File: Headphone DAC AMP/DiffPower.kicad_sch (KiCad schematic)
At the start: 0 parts

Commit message: Updating Changes
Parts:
- added U6: MCP1727-1802xSN, Package_SO:SOIC-8_3.9x4.9mm_P1.27mm, symbol Regulator_Linear:MCP1727-1802xSN
- added U7: MCP1727-3302xSN, Package_SO:SOIC-8_3.9x4.9mm_P1.27mm, symbol Regulator_Linear:MCP1727-3302xSN
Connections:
- new net: U7.1 (Vin), U7.2 (Vin)
- new net: U6.1 (Vin), U6.2 (Vin)
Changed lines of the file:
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@@
 	(generator_version "9.0")
 	(paper "A4")
+	(symbol
+		(lib_id "Regulator_Linear:MCP1727-3302xSN")
+		(at 71.12 99.06 0)
+		(unit 1)
+		(exclude_from_sim no)
+		(in_bom yes)
+		(on_board yes)
+		(dnp no)
+		(fields_autoplaced yes)
+		(property "Reference" "U7"
+			(at 71.12 88.9 0)
+			(effects
+				(font
+					(size 1.27 1.27)
+				)
+			)
+		)
+		(property "Value" "MCP1727-3302xSN"
+			(at 71.12 91.44 0)
+			(effects
+				(font
+					(size 1.27 1.27)
+				)
+			)
+		)
+		(property "Footprint" "Package_SO:SOIC-8_3.9x4.9mm_P1.27mm"
+			(at 71.12 74.93 0)
+			(effects
+				(font
+					(size 1.27 1.27)
+				)
+				(hide yes)
+			)
+		)
+		(property "Datasheet" "https://ww1.microchip.com/downloads/aemtest/APID/ProductDocuments/DataSheets/MCP1727-1.5A-Low-Voltage-Low-Quiescent-Current-LDO-Regulator-20001999D.pdf"
+			(at 71.12 77.47 0)
+			(effects
+				(font
+					(size 1.27 1.27)
+				)
+				(hide yes)
+			)
+		)
+		(property "Description" "1.5A, Low Voltage, Low Quiescent Current LDO Regulator, 2.3 - 6V Input, Fixed 3.3V Output, 330mV Dropout, SOIC-8"
+			(at 71.12 99.06 0)
+			(effects
+				(font
+					(size 1.27 1.27)
+				)
+				(hide yes)
+			)
+		)
+		(pin "8"
+		)
+		(pin "5"
+		)
+		(pin "2"
+		)
+		(pin "3"
+		)
+		(pin "4"
+		)
+		(pin "1"
+		)
+		(pin "7"
+		)
+		(pin "6"
+		)
+		(instances
+			(project ""
+				(path "/d034eddd-efbc-47be-a25c-37cbfbab4cd8/a76b11f7-fbf9-4331-be15-052b46a69f96"
+					(reference "U7")
+					(unit 1)
+				)
+			)
+		)
+	)
+	(symbol
+		(lib_id "Regulator_Linear:MCP1727-1802xSN")
+		(at 69.85 50.8 0)
+		(unit 1)
+		(exclude_from_sim no)
+		(in_bom yes)
+		(on_board yes)
+		(dnp no)
+		(fields_autoplaced yes)
+		(property "Reference" "U6"
+			(at 69.85 40.64 0)
+			(effects
+				(font
+					(size 1.27 1.27)
+				)
+			)
+		)
+		(property "Value" "MCP1727-1802xSN"
+			(at 69.85 43.18 0)
+			(effects
+				(font
+					(size 1.27 1.27)
+				)
+			)
+		)
+		(property "Footprint" "Package_SO:SOIC-8_3.9x4.9mm_P1.27mm"
+			(at 69.85 26.67 0)
+			(effects
+				(font
+					(size 1.27 1.27)
+				)
+				(hide yes)
+			)
+		)
+		(property "Datasheet" "https://ww1.microchip.com/downloads/aemtest/APID/ProductDocuments/DataSheets/MCP1727-1.5A-Low-Voltage-Low-Quiescent-Current-LDO-Regulator-20001999D.pdf"
+			(at 69.85 29.21 0)
+			(effects
+				(font
+					(size 1.27 1.27)
+				)
+				(hide yes)
+			)
+		)
+		(property "Description" "1.5A, Low Voltage, Low Quiescent Current LDO Regulator, 2.3 - 6V Input, Fixed 1.8V Output, 330mV Dropout, SOIC-8"
+			(at 69.85 50.8 0)
+			(effects
+				(font
+					(size 1.27 1.27)
+				)
+				(hide yes)
+			)
+		)
+		(pin "2"
+		)
+		(pin "8"
+		)
+		(pin "4"
+		)
+		(pin "5"
+		)
+		(pin "1"
+		)
+		(pin "3"
+		)
+		(pin "6"
+		)
+		(pin "7"
+		)
+		(instances
+			(project ""
+				(path "/d034eddd-efbc-47be-a25c-37cbfbab4cd8/a76b11f7-fbf9-4331-be15-052b46a69f96"
+					(reference "U6")
+					(unit 1)
+				)
+			)
+		)
+	)
 )

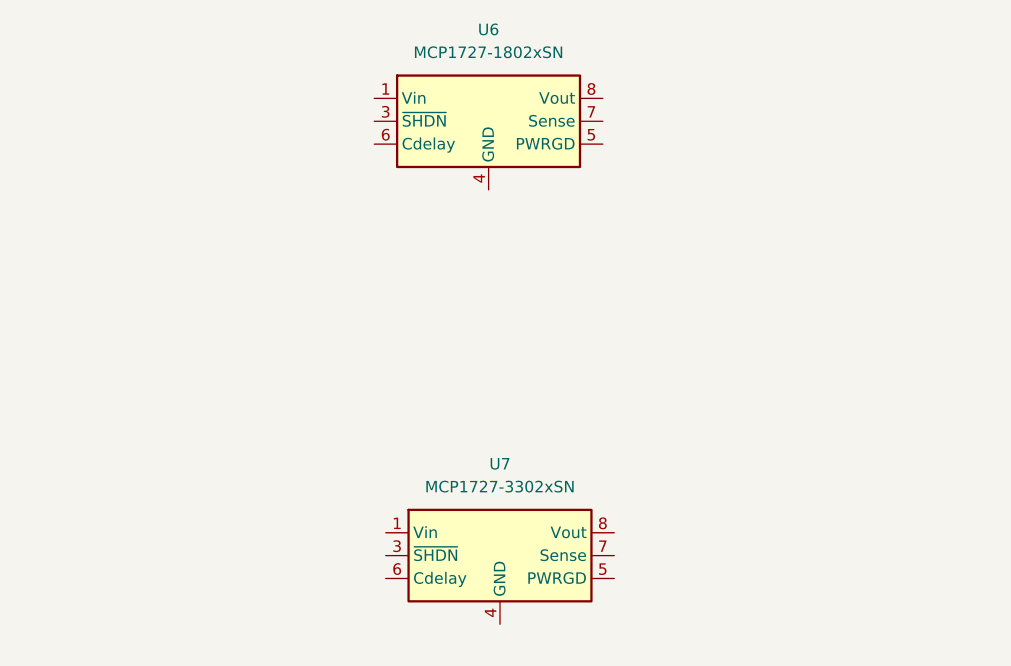
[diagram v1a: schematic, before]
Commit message: LDO Low Noise Rails 3.3 and 1.8
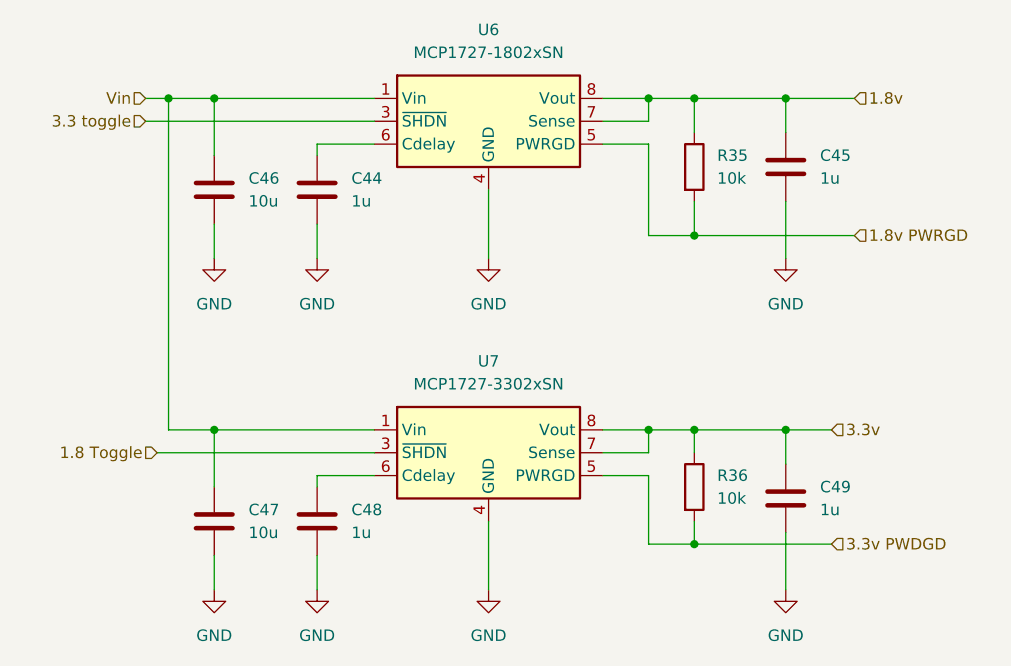
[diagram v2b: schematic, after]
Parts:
- added C44, C45, C48, C49: 1u, symbol Device:C
- added C46, C47: 10u, symbol Device:C
- added R35, R36: 10k, symbol Device:R
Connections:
- net Vin: now reaches U7.1 (Vin), U7.2 (Vin)
- net Vin: now also U6.1 (Vin), U6.2 (Vin), C46.1, C47.1
- net 1.8 Toggle: now reaches U7.3 (~{SHDN})
- net GND: now reaches U7.4 (GND)
- net GND: now also U6.4 (GND), C44.2, C45.2, C46.2, C47.2, C48.2, C49.2
- net 3.3v PWDGD: now reaches U7.5 (PWRGD)
- net 3.3v PWDGD: now also R36.2
- net at U7.6 (Cdelay): now also C48.1
- net 3.3v: now reaches U7.7 (Sense)
- net 3.3v: now also U7.8 (Vout), C49.1, R36.1
- net 3.3 toggle: now reaches U6.3 (~{SHDN})
- net 1.8v PWRGD: now reaches U6.5 (PWRGD)
- net 1.8v PWRGD: now also R35.2
- net at U6.6 (Cdelay): now also C44.1
- net 1.8v: now reaches U6.7 (Sense)
- net 1.8v: now also U6.8 (Vout), C45.1, R35.1
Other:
- moved on the sheet: U7

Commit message: Completed a significant amount of the power and routing
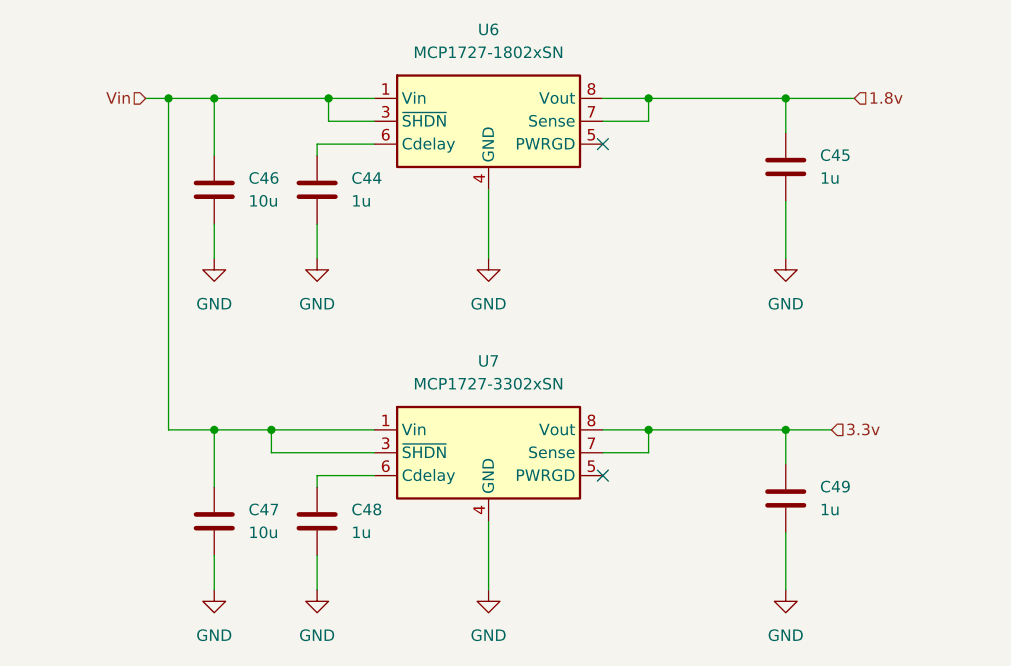
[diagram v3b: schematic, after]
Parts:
- removed R35, R36: 10k, symbol Device:R
- C44, C45, C46, C47, C48, C49: footprint (none) -> Capacitor_SMD:C_0805_2012Metric_Pad1.18x1.45mm_HandSolder
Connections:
- net 1.8 Toggle is gone; now on net Vin: U7.3 (~{SHDN})
- net 3.3 toggle is gone; now on net Vin: U6.3 (~{SHDN})
- net 1.8v PWRGD: no longer names the net of U6.5 (PWRGD)
- net 3.3v PWDGD: no longer names the net of U7.5 (PWRGD)
- no-connect marks 0 -> 2

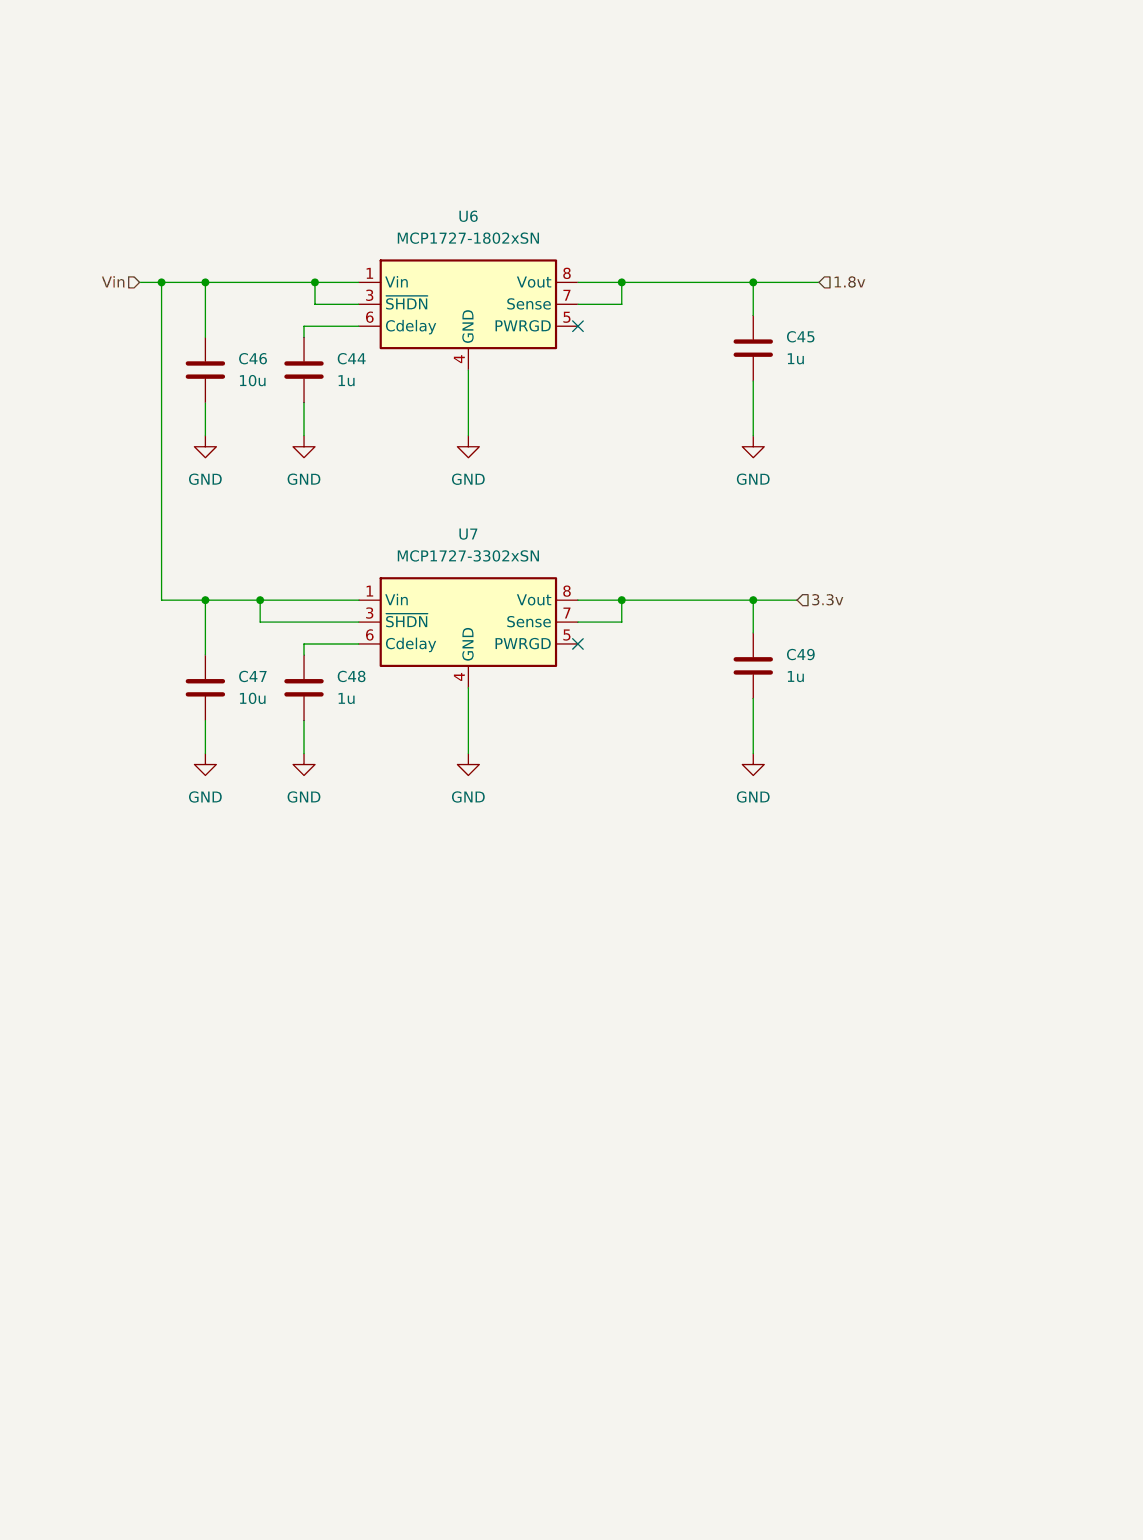
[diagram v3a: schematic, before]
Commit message: Added ground and 0.9v
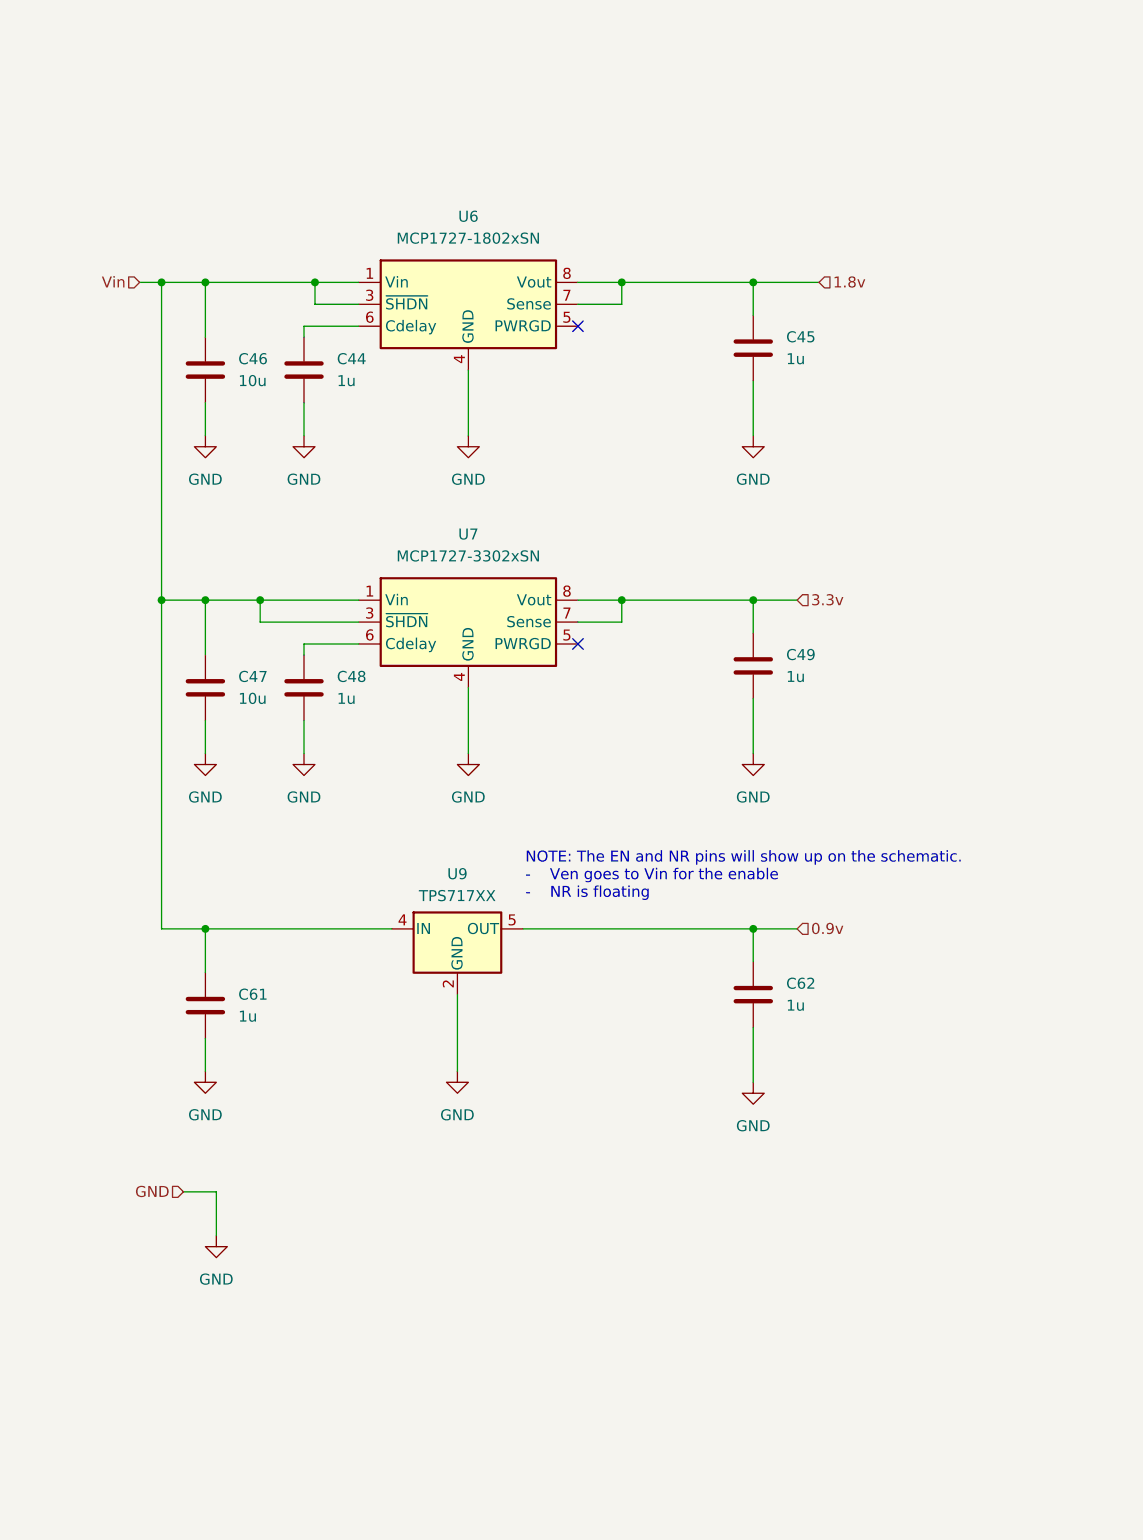
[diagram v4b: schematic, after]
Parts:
- added C61, C62: 1u, Capacitor_SMD:C_0805_2012Metric_Pad1.18x1.45mm_HandSolder, symbol Device:C
- added U9: TPS717XX, Package_TO_SOT_SMD:SOT-353_SC-70-5, symbol Regulator_Linear:TPS71518__SC70
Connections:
- net GND: now also C61.2, C62.2, U9.2 (GND)
- net Vin: now also C61.1, U9.4 (IN)
- new net 0.9v: C62.1, U9.5 (OUT)
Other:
- note added: "NOTE: The EN and NR pins will show up on the schematic. - Ven goes to Vin for the enable - NR is floating"

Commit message: Cleaned up shcematic more
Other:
- note added: "0.9V LDO"
- note added: "1.8V LDO"
- note added: "3.3V LDO"
- moved on the sheet: C44, C45, C46, C47, C48, C49, C61, C62, U6, U7, U9

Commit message: Cleaned Up and Annotated Schematic
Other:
- company: (none) -> Personal Project - Kettering University
- title: (none) -> Hi-Fidelity USB DAC Amplifier
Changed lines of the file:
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@@
 	(generator_version "9.0")
 	(paper "A4")
+	(title_block
+		(title "Hi-Fidelity USB DAC Amplifier")
+		(date "2025-11-19")
+		(rev "1.0")
+		(company "Personal Project - Kettering University")
+		(comment 1 "Designed by Dan Abidov & Luke Stirzinger")
+		(comment 2 "Based on XMOS Xu316 and ES9039Q2M")
+	)
 	(rectangle
 		(start 21.59 80.01)

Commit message: Hopefully my mistakes are not for naught
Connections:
- net 1.8v is gone; now on an unnamed net: C45.1, U6.7 (Sense), U6.8 (Vout)
- net Vin: no longer C61.1, U9.4 (IN)
- net at U9.1 (IN): now also C61.1, U9.3 (EN)
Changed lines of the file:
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@@
+	)
+	(junction
+		(at 59.69 148.59)
+		(diameter 0)
+		(color 0 0 0 0)
 	)
 	(junction
@@
 	(wire
 		(pts
-			(xy 40.64 148.59) (xy 35.56 148.59)
+			(xy 62.23 152.4) (xy 59.69 152.4)
 		)
 		(stroke
@@
 	(wire
 		(pts
+			(xy 59.69 152.4) (xy 59.69 148.59)
+		)
+		(stroke
+			(width 0)
+			(type default)
+		)
+	)
+	(wire
+		(pts
 			(xy 82.55 95.25) (xy 87.63 95.25)
 		)
@@
 	(wire
 		(pts
-			(xy 102.87 92.71) (xy 110.49 92.71)
+			(xy 40.64 135.89) (xy 114.3 135.89)
+		)
+		(stroke
+			(width 0)
+			(type default)
+		)
+	)
+	(wire
+		(pts
+			(xy 114.3 92.71) (xy 102.87 92.71)
 		)
 		(stroke
@@
 	(wire
 		(pts
+			(xy 40.64 148.59) (xy 40.64 135.89)
+		)
+		(stroke
+			(width 0)
+			(type default)
+		)
+	)
+	(wire
+		(pts
 			(xy 31.75 92.71) (xy 39.37 92.71)
 		)
@@
 	(wire
 		(pts
+			(xy 114.3 135.89) (xy 114.3 92.71)
+		)
+		(stroke
+			(width 0)
+			(type default)
+		)
+	)
+	(wire
+		(pts
+			(xy 59.69 148.59) (xy 40.64 148.59)
+		)
+		(stroke
+			(width 0)
+			(type default)
+		)
+	)
+	(wire
+		(pts
 			(xy 41.91 30.48) (xy 41.91 27.94)
 		)
@@
 	(wire
 		(pts
-			(xy 62.23 148.59) (xy 40.64 148.59)
+			(xy 62.23 148.59) (xy 59.69 148.59)
 		)
 		(stroke
@@
 		)
 	)
-	(hierarchical_label "1.8v"
-		(shape input)
-		(at 110.49 92.71 0)
-		(effects
-			(font
-				(size 1.27 1.27)
-			)
-			(justify left)
-		)
-	)
-	(hierarchical_label "Vin"
-		(shape input)
-		(at 35.56 148.59 180)
-		(effects
-			(font
-				(size 1.27 1.27)
-			)
-			(justify right)
-		)
-	)
 	(hierarchical_label "Vin"
 		(shape input)
@@
 		(pin "2"
 		)
-		(pin "1"
+		(pin "3"
 		)
 		(pin "5"
 		)
-		(pin "3"
-		)
-		(instances
+		(pin "1"
+		)
+		(instances
